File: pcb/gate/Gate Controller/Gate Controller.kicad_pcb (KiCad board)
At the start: 2 copper layers, 111.2 x 92.8 mm, 53 parts, among them IC1 MCP23009-E_SS, J11 Left Post, J13 AUX, J14 AUX, J17 AUX, J18 Power, J19 Fiber Power, J20 Driveway lights, J21 POE Camera, J23 Right Post, J25 Motor Controller, J26 Ethernet, J28 Pi, J3 CN7, J30 Post, J4 CN1, J6 Safety Stop, J8 Detect Gate Open, J9 Raspberry Controller, K1 EC2-5SNU, P1 pi, Q1 FDC6561AN, Q2 FDC6561AN, Q3 FDC6561AN, T1 STD40NF10

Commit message: latest updates
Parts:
- removed J13: AUX, TerminalBlock_Phoenix:TerminalBlock_Phoenix_PT_1.5-8-PVH-3.5
- removed J14: AUX, Connector_JST:JST_EH_S4B-EH_1x04_P2.50mm_Horizontal
- removed J23: Right Post, Connector_JST:JST_XH_PinSWAP
- removed J25: Motor Controller, Connector_JST:JST_XH_PinSWAP
- removed J28: Pi, Connector_JST:JST_XH_PinSWAP
- removed J30: Post, Connector_JST:JST_XH_PinSWAP
- added J10: RJ45_Shielded, Connector_RJ:RJ45_Amphenol_RJHSE5380, F.Cu at (108.2, 175.9)
- added J12: AUX, Connector_JST:JST_EH_S4B-EH_1x04_P2.50mm_Horizontal, F.Cu at (159.6, 114.5)
- added J15: AUX, Connector_JST:JST_EH_S4B-EH_1x04_P2.50mm_Horizontal, F.Cu at (80.5, 134.5)
- added J16: Power, TerminalBlock_TE-Connectivity:TerminalBlock_TE_282834-4_1x04_P2.54mm_Horizontal, F.Cu at (67.0, 113.7)
- added J22: Ethernet, Connector_RJ:RJ45_Amphenol_RJHSE5380, F.Cu at (137.5, 162.2)
- added J24: Pi, Connector_JST:JST_XH_S8B-XH-A_1x08_P2.50mm_Horizontal, F.Cu at (167.9, 171.4)
- added SW4: SW_Push, Button_Switch_THT:TS-D015, F.Cu at (76.2, 184.8)
- added U1: ~, Logos:QRCode Github Automation, F.Cu at (57.3, 198.0)
- added U2: ~, Logos:QRCode Github Automation, F.Cu at (90.0, 155.2)
- J11: value Left Post -> AUX; footprint Connector_JST:JST_XH_PinSWAP -> TerminalBlock_Phoenix:TerminalBlock_Phoenix_PT-1,5-8-3.5-H_1x08_P3.50mm_Horizontal
- J17: value AUX -> Fiber Power; footprint Connector_JST:JST_EH_S4B-EH_1x04_P2.50mm_Horizontal -> TerminalBlock_TE-Connectivity:TerminalBlock_TE_282834-4_1x04_P2.54mm_Horizontal
- J18: value Power -> Driveway lights
- J19: value Fiber Power -> POE Camera; footprint TerminalBlock_TE-Connectivity:TerminalBlock_TE_282834-4_1x04_P2.54mm_Horizontal -> Connector_RJ:RJ45_Amphenol_RJHSE5380
- J20: value Driveway lights -> RJ45_Shielded; footprint TerminalBlock_TE-Connectivity:TerminalBlock_TE_282834-4_1x04_P2.54mm_Horizontal -> Connector_RJ:RJ45_Amphenol_RJHSE5380
- J21: value POE Camera -> RJ45_Shielded
- J26: value Ethernet -> Post; footprint Connector_RJ:RJ45_Amphenol_RJHSE5380 -> Connector_JST:JST_XH_S8B-XH-A_1x08_P2.50mm_Horizontal
- J9: value Raspberry Controller -> RJ45_Shielded; footprint Connector_JST:JST_XH_PinSWAP -> Connector_RJ:RJ45_Amphenol_RJHSE5380
- moved J11 81.9 mm to (166.1, 131.2), turned to 90 degrees
- moved J19 79.0 mm to (137.5, 142.0)
- moved R12 52.1 mm to (124.7, 142.5)
- moved J26 49.0 mm to (161.0, 153.9)
- moved R9 46.8 mm to (124.7, 134.6)
- moved R10 45.3 mm to (124.7, 137.2)
- moved J21 45.2 mm to (137.5, 101.8)
- moved T1 42.4 mm to (124.7, 127.6)
- moved J20 40.6 mm to (137.5, 121.9), turned to -90 degrees
- moved J18 39.7 mm to (96.9, 131.9), turned to 0 degrees
- moved J17 36.6 mm to (67.0, 151.0)
- moved G3 33.7 mm to (92.8, 145.8), turned to 90 degrees
- moved R11 32.4 mm to (124.7, 139.9), turned to 180 degrees
- moved G1 27.1 mm to (76.2, 194.8)
- moved R8 25.2 mm to (124.7, 115.4)
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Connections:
- J11 pad 1: GATE_LED_12V -> L
- J11 pad 2: GND -> N
- J11 pad 3: CN1_24v(FL) -> E
- J11 pad 4: CN1_(FL)- -> L1
- J11 pad 5: GND -> N
- J11 pad 6: START -> L2
- J11 pad 7: PH1 -> N
- J11 pad 8: ANTENNA+ -> E
- J17 pad 1: GND -> +5v
- J17 pad 2: 5v -> GND
- J17 pad 3: Net-(J17-Pad3) -> +5v
- J18 pad 1: GND -> W1
- J18 pad 2: +12V -> GND
- J18 pad 3: GND -> +12V
- J18 pad 4: 5v -> 3V3
- J19 pad 1: +12V -> Net-(J19-Pad1)
- J19 pad 2: GND -> Net-(J19-Pad2)
- J19 pad 3: +12V -> Net-(J19-Pad3)
- J19 pad 4: GND -> +12V
- J20 pad 1: W1 -> +12V
- J20 pad 2: GND -> GATE_LED_COM
- J20 pad 3: +12V -> CN1_24v(FL)
- J20 pad 4: 3V3 -> unconnected-(J20-Pad4)
- J21 pad 1: Net-(J21-Pad1) -> +12V
- J21 pad 2: Net-(J21-Pad2) -> GATE_LED_COM
- J21 pad 3: Net-(J21-Pad3) -> CN1_24v(FL)
- J21 pad 4: +12V -> SCL1
- J21 pad 5: +12V -> SDA1
- J21 pad 6: Net-(J21-Pad6) -> GND
- J21 pad 7: GND -> REED LEFT
- J21 pad 8: GND -> 3V3
- J26 pad 1: Net-(J21-Pad1) -> GATE_LED_12V
- J26 pad 2: Net-(J21-Pad2) -> Net-(J24-Pin_2)
- J26 pad 3: Net-(J21-Pad3) -> CN1_24v(FL)
- J26 pad 6: Net-(J21-Pad6) -> GND
- J26 pad 7: unconnected-(J26-Pad7) -> REED RIGHT
- J26 pad 8: unconnected-(J26-Pad8) -> 3V3
- J9 pad 1: GATE_LED_12V -> +12v
- J9 pad 2: GND -> GATE_LED_COM
- P1 pad 2: 5v -> +5v
- P1 pad 4: 5v -> +5v
- Q3 pad 6: Net-(J17-Pad3) -> Net-(J15-Pin_3)
- T1 pad 2: +12V -> GATE_LED_COM
- T1 pad 3: GATE_LED_12V -> GND
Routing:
- net GATE_LED_COM: track 0.00 -> 115.8 mm
- net GATE_LED_12V: track 111.2 -> 20.9 mm, vias 0 -> 1
- net +5v: track 0.00 -> 72.4 mm
- net Net-(J15-Pin_3): track 0.00 -> 66.7 mm, vias 0 -> 2
- net +12v: track 0.00 -> 65.8 mm
- net GND: track 0.00 -> 60.7 mm, vias 61 -> 57
- net W1: track 101.5 -> 41.4 mm
- net 5v: track 60.0 -> 0.00 mm
- net SDA1: track 69.8 -> 123.1 mm, vias 0 -> 2
- net START: track 63.2 -> 115.2 mm
- net REED LEFT: track 22.2 -> 63.6 mm
- net +12V: track 184.6 -> 145.0 mm
- net ANTENNA+: track 49.8 -> 86.7 mm
- net PEDST: track 18.3 -> 50.8 mm
- net 3V3: track 235.0 -> 204.6 mm, vias 0 -> 3
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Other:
- board size 111.2 x 92.8 mm -> 124.5 x 104.2 mm
- board text added: "AUX LIGHTS"
- board text added: "CAMERA"
- board text added: "RIGHT POST"
- board text added: "SEA MOTOR"
- board text added: "WAN"
- board text added: "© 2024"
- board text removed: "© 2022"

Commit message: Updated gate controller pcb to 2024.1.0
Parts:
- SW4: value SW_Push -> START
- moved J21 4.66 mm to (137.2, 97.1)
- moved J22 4.66 mm to (137.2, 157.5)
- moved J20 4.66 mm to (137.2, 117.3)
- moved J19 4.66 mm to (137.2, 137.4)
- moved J8 1.30 mm to (77.5, 174.2)
- moved J3 1.04 mm to (95.8, 174.2)
- moved R4 0.51 mm to (99.5, 179.1)
- moved R3 0.50 mm to (99.5, 181.6)
- moved R7 0.35 mm to (89.9, 179.3)
- moved R5 0.30 mm to (95.9, 180.5)
- moved R6 0.30 mm to (93.5, 180.5)
- moved J6 0.10 mm to (86.5, 174.2)
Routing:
- net GATE_LED_COM: track 115.8 -> 129.2 mm, vias 0 -> 1
- net SDA1: track 123.1 -> 110.4 mm, vias 2 -> 1
- net REED LEFT: track 63.6 -> 74.4 mm
- net Net-(J15-Pin_3): track 66.7 -> 58.3 mm
- net PEDST: track 50.8 -> 57.2 mm
- net CN1_24v(FL): track 142.1 -> 146.7 mm
- net REED RIGHT: track 52.8 -> 57.4 mm
- net 3V3: track 204.6 -> 208.4 mm
- net Net-(J19-Pad2): track 25.9 -> 22.4 mm
- net SCL1: track 87.8 -> 91.3 mm
- net STOP: track 43.6 -> 46.9 mm
- net Rpi15: track 56.3 -> 59.5 mm
- net unconnected-(J22-Pad4): track 0.00 -> 2.17 mm
- net Net-(IC1-GP0): track 36.1 -> 37.5 mm
- net Net-(IC1-GP6): track 18.1 -> 19.3 mm
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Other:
- board size 124.5 x 104.2 mm -> 124.5 x 109.5 mm
- board text added: "2024.1.0"
- board text removed: "© 2024"

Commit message: Updated pcb
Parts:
- SW4: value START -> SW_Push
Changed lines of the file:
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@@
 		)
 		(property "Value" "RJ45_Shielded"
-			(at 3.56 9.5 360)
+			(at 3.56 9.5 0)
 			(layer "F.Fab")
 			(effects
@@
 		)
 		(fp_text user "${REFERENCE}"
-			(at 3.56 -6 360)
+			(at 3.56 -6 0)
 			(layer "F.Fab")
 			(effects
@@
 		)
 		(property "Value" "RJ45_Shielded"
-			(at 3.56 9.5 360)
+			(at 3.56 9.5 0)
 			(layer "F.Fab")
 			(effects
@@
 		)
 		(fp_text user "${REFERENCE}"
-			(at 3.56 -6 360)
+			(at 3.56 -6 0)
 			(layer "F.Fab")
 			(effects
@@
 			)
 		)
-		(property "Value" "START"
+		(property "Value" "SW_Push"
 			(at 0 6 90)
 			(unlocked yes)
@@
 		(at 76.25 194.75)
 		(property "Reference" "G1"
-			(at 1.27 -3.81 360)
+			(at 1.27 -3.81 0)
 			(layer "F.SilkS")
 			(hide yes)
@@
 		)
 		(property "Value" "LOGO"
-			(at 0 3.81 360)
+			(at 0 3.81 0)
 			(layer "F.SilkS")
 			(hide yes)
@@
 		)
 		(property "Footprint" "OneTouch_Logo:onetouchlogo"
-			(at 0 0 360)
+			(at 0 0 0)
 			(layer "F.Fab")
 			(hide yes)
@@
 		)
 		(property "Datasheet" ""
-			(at 0 0 360)
+			(at 0 0 0)
 			(layer "F.Fab")
 			(hide yes)
@@
 		)
 		(property "Description" ""
-			(at 0 0 360)
+			(at 0 0 0)
 			(layer "F.Fab")
 			(hide yes)

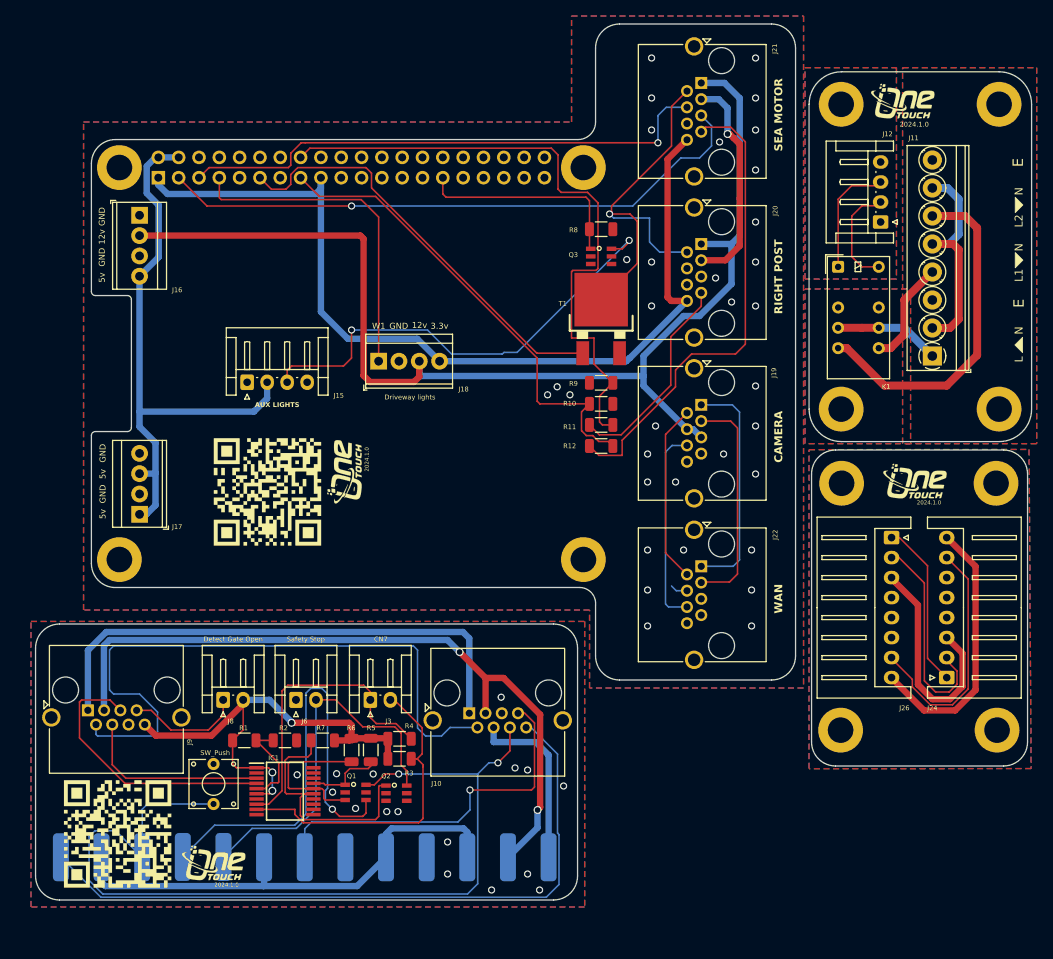
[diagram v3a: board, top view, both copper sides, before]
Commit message: reworked to add i2c pullups and reduces unusedd components
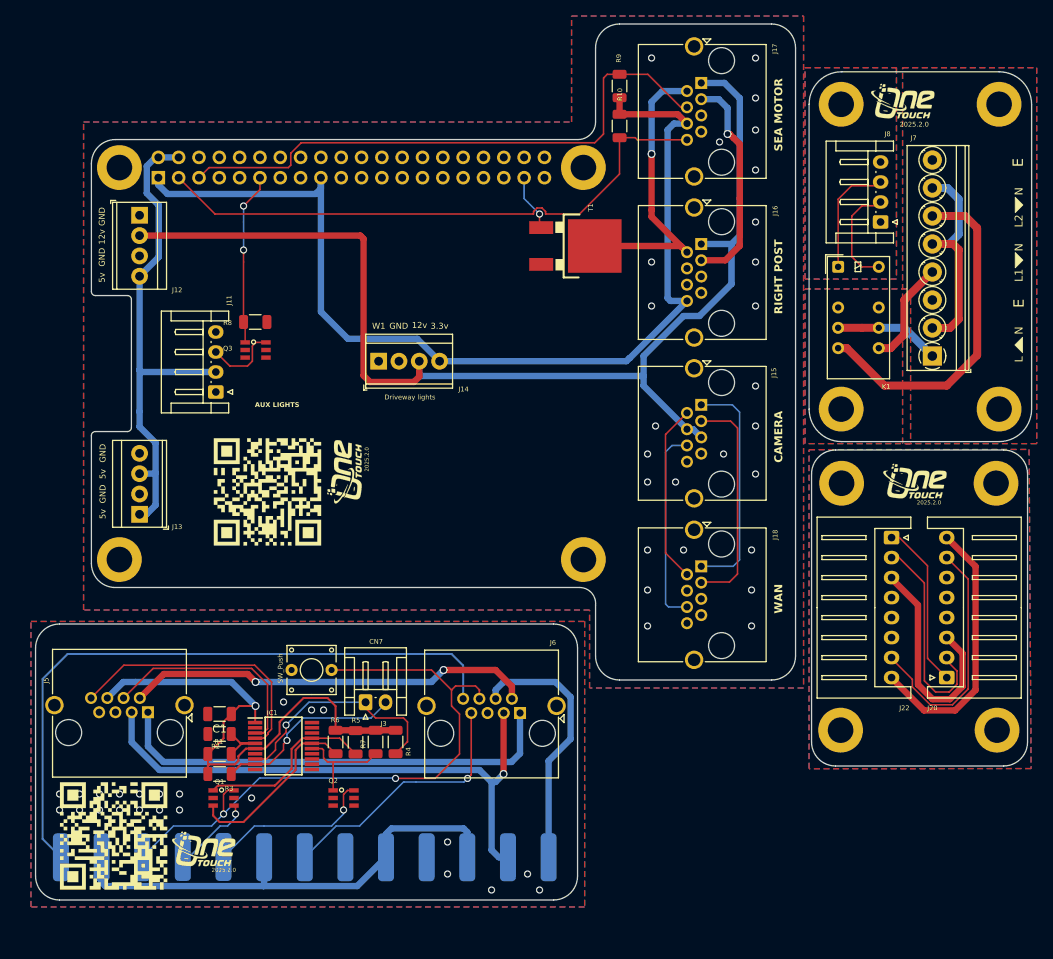
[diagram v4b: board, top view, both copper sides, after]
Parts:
- removed the J6 at (86.5, 174.2)
- removed the J8 at (77.5, 174.2)
- removed R11, R12: 1K, Resistor_SMD:R_1206_3216Metric
- added C1: 0.1uF, Capacitor_SMD:C_1206_3216Metric, F.Cu at (77.0, 176.0)
- R10, R9: value 10K -> 1.8K
- moved R8 44.8 mm to (81.5, 127.0)
- moved Q3 44.8 mm to (81.5, 130.5)
- moved R9 37.2 mm to (127.0, 97.5), turned to -90 degrees
- moved R10 34.8 mm to (127.0, 102.5), turned to 90 degrees
- moved R3 22.6 mm to (77.0, 183.5)
- moved SW1 18.8 mm to (88.5, 170.5), turned to 180 degrees
- moved Q1 16.5 mm to (77.5, 186.5)
- moved T1 10.9 mm to (120.5, 117.5), turned to -90 degrees
- moved R2 8.21 mm to (77.0, 178.5), turned to 180 degrees
- moved J5 7.51 mm to (68.0, 175.8), turned to 180 degrees
- moved Q2 6.63 mm to (92.5, 186.5)
- moved R7 6.60 mm to (96.5, 179.5), turned to 90 degrees
- moved J6 6.35 mm to (114.6, 175.9), turned to 180 degrees
- moved IC1 5.65 mm to (85.0, 180.0)
- moved J11 4.10 mm to (76.5, 135.8), turned to 90 degrees
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- renumbered J15 to J11, J16 to J12, J17 to J13, J18 to J14, J19 to J15, J20 to J16, J21 to J17, J22 to J18, J24 to J20, J26 to J22, J9 to J5, J10 to J6, J11 to J7, J12 to J8, SW4 to SW1
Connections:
- J16 pad 7: REED RIGHT -> unconnected-(J16-Pad7)
- J16 pad 8: 3V3 -> unconnected-(J16-Pad8)
- J17 pad 5: SDA1 -> GND
- J17 pad 6: GND -> 3V3
- J17 pad 7: REED LEFT -> GND
- J17 pad 8: 3V3 -> SDA1
- J20 pad 7: REED RIGHT -> unconnected-(J20-Pin_7-Pad7)
- J20 pad 8: 3V3 -> unconnected-(J20-Pin_8-Pad8)
- J22 pad 7: REED RIGHT -> unconnected-(J22-Pin_7-Pad7)
- J22 pad 8: 3V3 -> unconnected-(J22-Pin_8-Pad8)
- J5 pad 5: SDA1 -> GND
- J5 pad 6: GND -> 3V3
- J5 pad 7: REED LEFT -> GND
- J5 pad 8: 3V3 -> SDA1
- P1 pad 29: Rpi29 -> unconnected-(P1-Pin_29-Pad29)
- P1 pad 37: unconnected-(P1-Pin_37-Pad37) -> Rpi37
- Q3 pad 1: Rpi29 -> Rpi11
- R10 pad 1: GND -> SDA1
- R10 pad 2: Rpi15 -> 3V3
- R8 pad 1: Rpi29 -> Rpi11
- R9 pad 1: GND -> SCL1
- R9 pad 2: Rpi16 -> 3V3
- T1 pad 1: Rpi11 -> Rpi37
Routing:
- net Rpi16: track 79.8 -> 0.00 mm
- net REED LEFT: track 74.4 -> 0.00 mm
- net Rpi15: track 59.5 -> 0.00 mm
- net REED RIGHT: track 57.4 -> 0.00 mm
- net Net-(J11-Pin_3): track 58.3 -> 9.33 mm, vias 2 -> 0
- net PEDST: track 57.2 -> 10.2 mm
- net W1: track 41.4 -> 0.00 mm
- net GATE_LED_COM: track 129.2 -> 88.6 mm, vias 1 -> 3
- net START: track 115.2 -> 78.5 mm
- net Rpi11: track 53.5 -> 21.5 mm, vias 0 -> 2
- net (no net): track 0.00 -> 31.0 mm
- net Rpi29: track 26.8 -> 0.00 mm
- net STOP: track 46.9 -> 21.2 mm, vias 0 -> 1
- net 3V3: track 208.4 -> 229.3 mm, vias 3 -> 1
- net CN1_24v(FL): track 146.7 -> 127.2 mm, vias 3 -> 2
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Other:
- board text added: "${REVISION}"
- board text removed: "2024.1.0"

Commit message: Update with latest changes to fix comms issues
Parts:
- removed U1: ~, Logos:QRCode Github Automation
- IC1: footprint MCP23009-E_SS:SOP65P780X200-20N -> MCP23009_E_SS:SOP65P780X200-20N
- J12, J13, J14: footprint TerminalBlock_TE-Connectivity:TerminalBlock_TE_282834-4_1x04_P2.54mm_Horizontal -> Connector_JST:JST_EH_S4B-EH_1x04_P2.50mm_Horizontal
- P1: footprint Connector_PinSocket_2.54mm:PinSocket_2x20_P2.54mm_Vertical -> Connector_PinSocket_2.54mm:PinSocket_2x10_P2.54mm_Vertical_SMD
- SW1: value SW_Push -> START
- moved G1 25.3 mm to (79.2, 168.1)
- moved P1 12.7 mm to (81.9, 107.5)
- moved J12 7.74 mm to (68.5, 121.2), turned to 90 degrees
- moved J13 1.58 mm to (68.5, 150.6)
- moved J14 1.35 mm to (96.7, 130.6)
- moved G3 0.89 mm to (93.6, 145.8)
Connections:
- C1 pad 1: 3V3 -> Net-(IC1-VSS)
- C1 pad 2: GND -> 3V3
- IC1 pad 20: GND -> Net-(IC1-VSS)
- P1 pad 15: Rpi15 -> unconnected-(P1-Pin_15-Pad15)
- P1 pad 16: Rpi16 -> unconnected-(P1-Pin_16-Pad16)
- T1 pad 1: Rpi37 -> Rpi13
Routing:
- net GND: track 60.7 -> 0.00 mm, vias 49 -> 69
- net W1: track 0.00 -> 59.6 mm, vias 0 -> 1
- net 3V3: track 229.3 -> 183.8 mm
- net Rpi13: track 0.00 -> 34.8 mm, vias 0 -> 1
- net (no net): track 31.0 -> 0.00 mm
- net Rpi11: track 21.5 -> 48.5 mm, vias 2 -> 1
- net Net-(IC1-VSS): track 0.00 -> 20.4 mm, vias 0 -> 2
- net START: track 78.5 -> 87.9 mm
- net +12V: track 145.9 -> 137.6 mm
- net SCL1: track 100.7 -> 108.7 mm, vias 0 -> 1
- net Rpi37: track 7.12 -> 0.00 mm, vias 1 -> 0
- net +5v: track 63.4 -> 67.1 mm
- net Net-(IC1-GP6): track 22.9 -> 24.7 mm
- net ANTENNA+: track 81.8 -> 80.4 mm
- net PH1: track 32.8 -> 33.4 mm
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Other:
- outline, holes or cut-outs redrawn
